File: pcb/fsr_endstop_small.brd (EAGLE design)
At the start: 27.9 x 30.5 mm, 31 parts, among them U1 ATTINY461

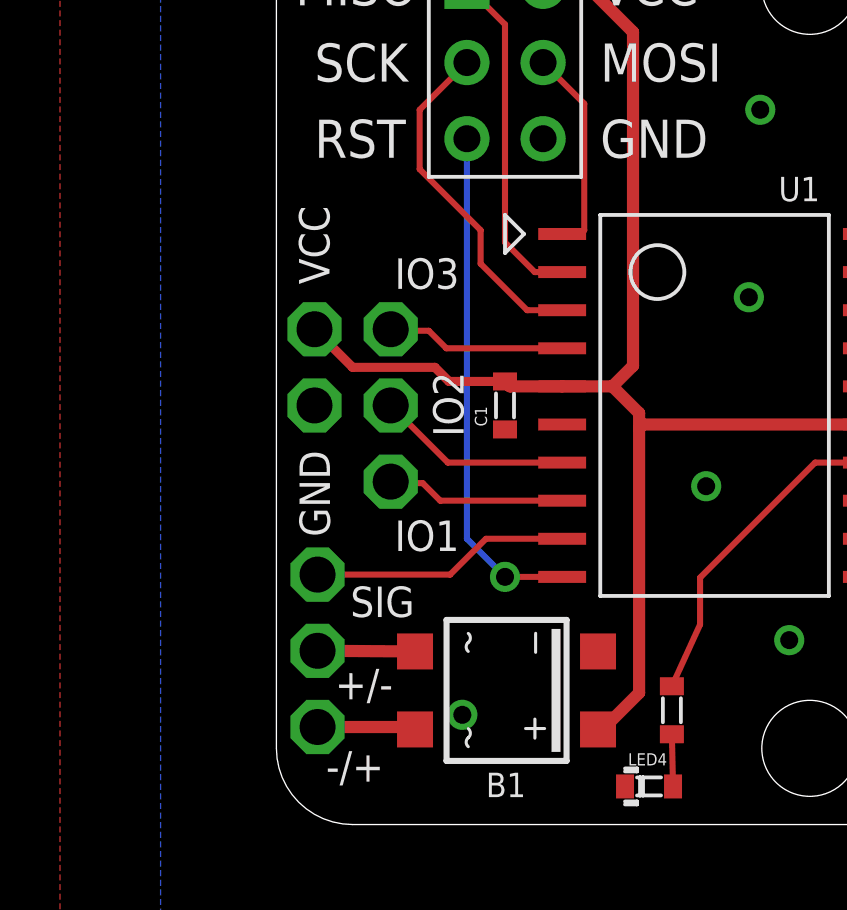
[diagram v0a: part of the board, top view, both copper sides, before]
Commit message: Revision 1.2 includes three jumpers for modifying settings.
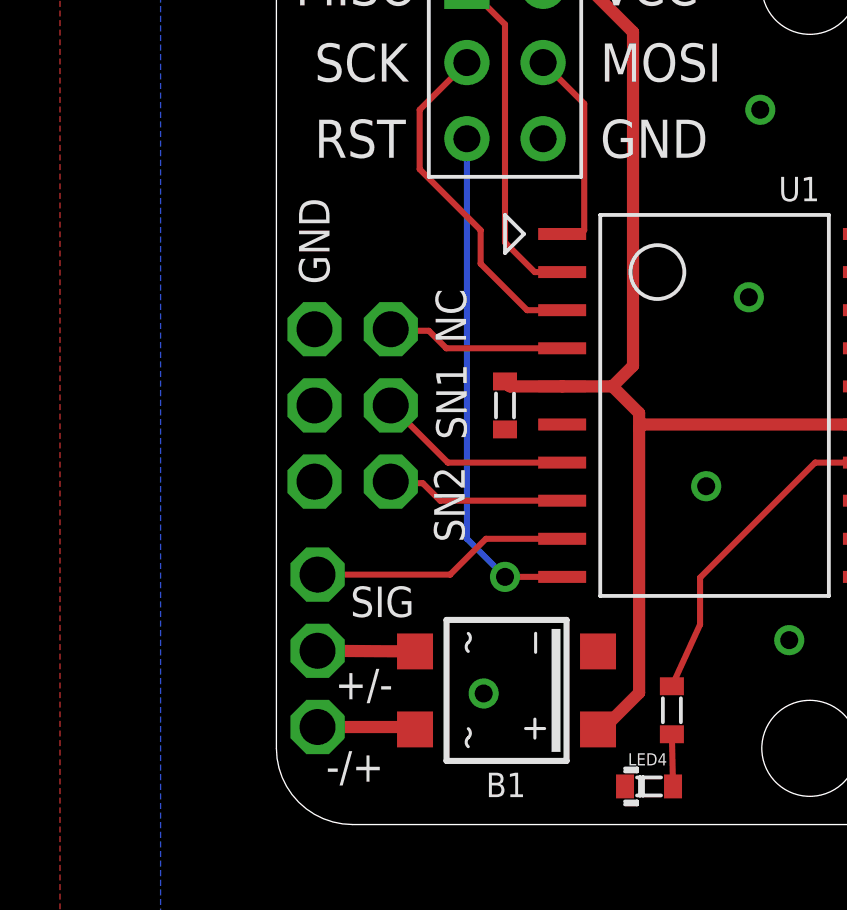
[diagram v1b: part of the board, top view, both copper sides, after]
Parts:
- removed VCC: PIN1.2MM, _sg_lib:PIN_1.2MM
- added GND1, GND2: PIN1.2MM, _sg_lib:PIN_1.2MM
- R1, R2, R3, R4: value (none) -> 100
- moved GND 2.54 mm to (14.0, 29.2), turned to 90 degrees
- renumbered IO1 to SN2, IO2 to SN1, IO3 to NC
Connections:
- net GND: now also GND1.P$1, GND2.P$1
- net V+: no longer VCC.P$1
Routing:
- net V+: track 74.1 -> 67.1 mm
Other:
- board text added: "rev1.2"
- board text removed: "rev1.1"
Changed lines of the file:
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@@
 <text x="25.8064" y="17.78" size="2.1844" layer="22" font="vector" rot="MR90">FSR Endstop</text>
 <text x="21.844" y="17.78" size="2.1844" layer="22" font="vector" rot="MR90">Controller</text>
-<text x="18.1356" y="17.78" size="2.1844" layer="22" font="vector" rot="MR90">rev1.1</text>
+<text x="18.1356" y="17.78" size="2.1844" layer="22" font="vector" rot="MR90">rev1.2</text>
 </plain>
 <attributes>
@@
 <element name="FSR3A" library="_sg_lib" package="PIN_1.2MM" value="PIN1.2MM" x="38.1" y="17.78" smashed="yes" rot="R180"/>
 <element name="AVR1" library="_sg_misc" package="AVR6" value="AVR6" x="20.32" y="38.1" smashed="yes"/>
-<element name="C1" library="_sg_lib" package="0603" value="1uF" x="20.32" y="26.67" rot="R90"/>
+<element name="C1" library="_sg_lib" package="0603" value="1uF" x="20.32" y="26.67" smashed="yes" rot="R90">
+<attribute name="NAME" x="20.4312" y="28.129" size="0.4064" layer="25" font="vector" rot="R90"/>
+<attribute name="NAME" x="20.22" y="25.87" size="0.3048" layer="51" font="vector" rot="R90"/>
+<attribute name="VALUE" x="20.62" y="25.87" size="0.3048" layer="51" font="vector" rot="R90"/>
+</element>
 <element name="LED1" library="_sg_lib" package="0603_DIODE" value="LED0603" x="36.195" y="36.195" rot="R90"/>
 <element name="LED2" library="_sg_lib" package="0603_DIODE" value="LED0603" x="36.195" y="27.305" smashed="yes" rot="R90">
@@
 <element name="LED3" library="_sg_lib" package="0603_DIODE" value="LED0603" x="36.195" y="18.415" rot="R90"/>
 <element name="LED4" library="_sg_lib" package="0603_DIODE" value="LED0603" x="25.1206" y="13.97"/>
-<element name="R1" library="_sg_lib" package="0603" value="" x="36.195" y="38.735" smashed="yes" rot="R270">
+<element name="R1" library="_sg_lib" package="0603" value="100" x="36.195" y="38.735" smashed="yes" rot="R270">
 <attribute name="NAME" x="35.0678" y="39.3334" size="0.4064" layer="25" font="vector" rot="R270"/>
 <attribute name="NAME" x="36.295" y="39.535" size="0.3048" layer="51" font="vector" rot="R270"/>
 <attribute name="VALUE" x="35.895" y="39.535" size="0.3048" layer="51" font="vector" rot="R270"/>
 </element>
-<element name="R2" library="_sg_lib" package="0603" value="" x="36.195" y="29.845" smashed="yes" rot="R270">
+<element name="R2" library="_sg_lib" package="0603" value="100" x="36.195" y="29.845" smashed="yes" rot="R270">
 <attribute name="NAME" x="35.1694" y="30.037" size="0.4064" layer="25" font="vector" rot="R270"/>
 <attribute name="NAME" x="36.295" y="30.645" size="0.3048" layer="51" font="vector" rot="R270"/>
 <attribute name="VALUE" x="35.895" y="30.645" size="0.3048" layer="51" font="vector" rot="R270"/>
 </element>
-<element name="R3" library="_sg_lib" package="0603" value="" x="36.195" y="20.955" smashed="yes" rot="R270">
+<element name="R3" library="_sg_lib" package="0603" value="100" x="36.195" y="20.955" smashed="yes" rot="R270">
 <attribute name="NAME" x="35.0678" y="20.9438" size="0.4064" layer="25" font="vector" rot="R270"/>
 <attribute name="NAME" x="36.295" y="21.755" size="0.3048" layer="51" font="vector" rot="R270"/>
 <attribute name="VALUE" x="35.895" y="21.755" size="0.3048" layer="51" font="vector" rot="R270"/>
 </element>
-<element name="R4" library="_sg_lib" package="0603" value="" x="25.8826" y="16.51" smashed="yes" rot="R270">
+<element name="R4" library="_sg_lib" package="0603" value="100" x="25.8826" y="16.51" smashed="yes" rot="R270">
 <attribute name="NAME" x="24.7554" y="16.8036" size="0.4064" layer="25" font="vector" rot="R270"/>
 <attribute name="NAME" x="25.9826" y="17.31" size="0.3048" layer="51" font="vector" rot="R270"/>
@@
 <attribute name="VALUE" x="38.4" y="22.06" size="0.3048" layer="51" font="vector" rot="R90"/>
 </element>
-<element name="IO1" library="_sg_lib" package="PIN_1.2MM" value="PIN1.2MM" x="16.51" y="24.13" smashed="yes">
-<attribute name="NAME" x="18.796" y="22.8346" size="1.016" layer="21" font="vector" rot="R180"/>
-</element>
-<element name="IO2" library="_sg_lib" package="PIN_1.2MM" value="PIN1.2MM" x="16.51" y="26.67" smashed="yes">
-<attribute name="NAME" x="18.9404" y="25.63" size="1.016" layer="21" font="vector" rot="R90"/>
-</element>
-<element name="IO3" library="_sg_lib" package="PIN_1.2MM" value="PIN1.2MM" x="16.51" y="29.21" smashed="yes">
-<attribute name="NAME" x="18.796" y="31.5722" size="1.016" layer="21" font="vector" rot="R180"/>
-</element>
-<element name="GND" library="_sg_lib" package="PIN_1.2MM" value="PIN1.2MM" x="13.97" y="26.67" rot="R270"/>
-<element name="VCC" library="_sg_lib" package="PIN_1.2MM" value="PIN1.2MM" x="13.97" y="29.21" rot="R90"/>
+<element name="SN2" library="_sg_lib" package="PIN_1.2MM" value="PIN1.2MM" x="16.51" y="24.13" smashed="yes">
+<attribute name="NAME" x="17.9578" y="24.638" size="1.016" layer="21" font="vector" rot="R270"/>
+</element>
+<element name="SN1" library="_sg_lib" package="PIN_1.2MM" value="PIN1.2MM" x="16.51" y="26.67" smashed="yes">
+<attribute name="NAME" x="19.042" y="25.5284" size="1.016" layer="21" font="vector" rot="R90"/>
+</element>
+<element name="NC" library="_sg_lib" package="PIN_1.2MM" value="PIN1.2MM" x="16.51" y="29.21" smashed="yes">
+<attribute name="NAME" x="18.0086" y="30.5562" size="1.016" layer="21" font="vector" rot="R270"/>
+</element>
+<element name="GND2" library="_sg_lib" package="PIN_1.2MM" value="PIN1.2MM" x="13.97" y="26.67" smashed="yes" rot="R270"/>
+<element name="GND" library="_sg_lib" package="PIN_1.2MM" value="PIN1.2MM" x="13.97" y="29.21" rot="R90"/>
 <element name="C2" library="_sg_lib" package="0603" value="1uF" x="34.29" y="26.67" smashed="yes" rot="R270">
 <attribute name="NAME" x="34.3012" y="25.1364" size="0.4064" layer="25" font="vector"/>
@@
 </element>
 <element name="U$1" library="SparkFun-Aesthetics" package="OSHW-LOGO-M" value="" x="31.1912" y="27.0256" rot="MR90"/>
+<element name="GND1" library="_sg_lib" package="PIN_1.2MM" value="PIN1.2MM" x="13.97" y="24.13" smashed="yes"/>
 </elements>
 <signals>
@@
 <contactref element="R6" pad="2"/>
 <contactref element="R7" pad="2"/>
-<contactref element="VCC" pad="P$1"/>
 <contactref element="C2" pad="2"/>
 <wire x1="24.7904" y1="17.0896" x2="24.7904" y2="25.908" width="0.4064" layer="1"/>
@@
 <wire x1="32.385" y1="26.035" x2="34.125" y2="26.035" width="0.4064" layer="1"/>
 <wire x1="34.125" y1="26.035" x2="34.29" y2="25.87" width="0.4064" layer="1"/>
-<wire x1="20.32" y1="27.47" x2="18.4532" y2="27.47" width="0.3048" layer="1"/>
-<wire x1="18.4532" y1="27.47" x2="17.9832" y2="27.94" width="0.3048" layer="1"/>
-<wire x1="17.9832" y1="27.94" x2="15.24" y2="27.94" width="0.3048" layer="1"/>
-<wire x1="15.24" y1="27.94" x2="13.97" y2="29.21" width="0.3048" layer="1"/>
 <wire x1="34.29" y1="25.87" x2="34.3788" y2="25.87" width="0.3048" layer="1"/>
 <wire x1="34.3788" y1="25.87" x2="34.9504" y2="25.2984" width="0.3048" layer="1"/>
@@
 <contactref element="FSR2A" pad="P$1"/>
 <contactref element="FSR1A" pad="P$1"/>
-<contactref element="GND" pad="P$1"/>
+<contactref element="GND2" pad="P$1"/>
 <contactref element="LED1" pad="-"/>
 <contactref element="LED2" pad="-"/>
@@
 <via x="27.0256" y="23.9776" extent="1-16" drill="0.6"/>
 <via x="28.448" y="30.2768" extent="1-16" drill="0.6"/>
-<via x="18.8976" y="16.3576" extent="1-16" drill="0.6"/>
+<via x="19.6088" y="17.0688" extent="1-16" drill="0.6"/>
 <via x="34.036" y="24.5872" extent="1-16" drill="0.6"/>
 <via x="28.829" y="36.5252" extent="1-16" drill="0.6"/>
 <contactref element="B1" pad="-"/>
+<contactref element="GND" pad="P$1"/>
+<contactref element="GND1" pad="P$1"/>
 </signal>
 <signal name="N$1">
@@
 <signal name="N$16">
 <contactref element="U1" pad="P$8"/>
-<contactref element="IO1" pad="P$1"/>
+<contactref element="SN2" pad="P$1"/>
 <wire x1="22.225" y1="23.495" x2="18.161" y2="23.495" width="0.2032" layer="1"/>
 <wire x1="18.161" y1="23.495" x2="17.5768" y2="24.0792" width="0.2032" layer="1"/>
@@
 <signal name="N$17">
 <contactref element="U1" pad="P$7"/>
-<contactref element="IO2" pad="P$1"/>
+<contactref element="SN1" pad="P$1"/>
 <wire x1="22.225" y1="24.765" x2="18.415" y2="24.765" width="0.2032" layer="1"/>
 <wire x1="18.415" y1="24.765" x2="16.51" y2="26.67" width="0.2032" layer="1"/>
@@
 <signal name="N$15">
 <contactref element="U1" pad="P$4"/>
-<contactref element="IO3" pad="P$1"/>
+<contactref element="NC" pad="P$1"/>
 <wire x1="22.225" y1="28.575" x2="18.3642" y2="28.575" width="0.2032" layer="1"/>
 <wire x1="18.3642" y1="28.575" x2="17.78" y2="29.1592" width="0.2032" layer="1"/>
